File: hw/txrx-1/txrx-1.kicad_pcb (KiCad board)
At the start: 2 copper layers, 94 parts, among them J1 Conn_Coaxial, J2 Power, J4 Conn_01x07, U1 SN74CBT3253, U2 LM4562, U3 LM4562, U4 Si5351A-B-GT, U41 LM4562, U42 LM4562, U43 SN74CBT3253

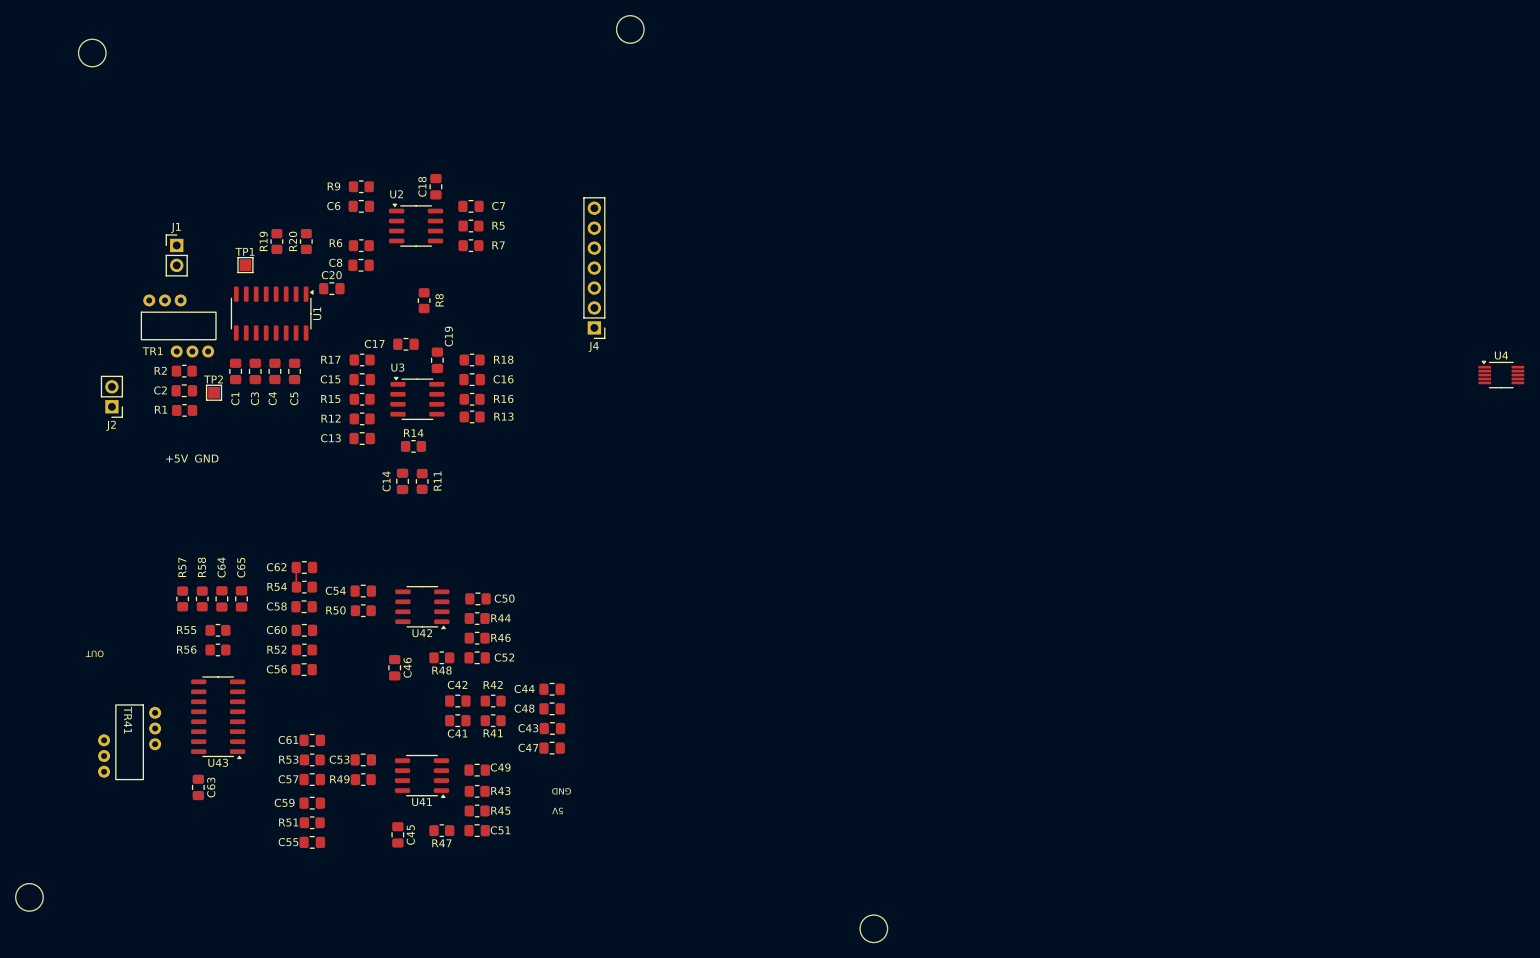
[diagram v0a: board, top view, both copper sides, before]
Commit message: Initial PCB layout for TXRX board
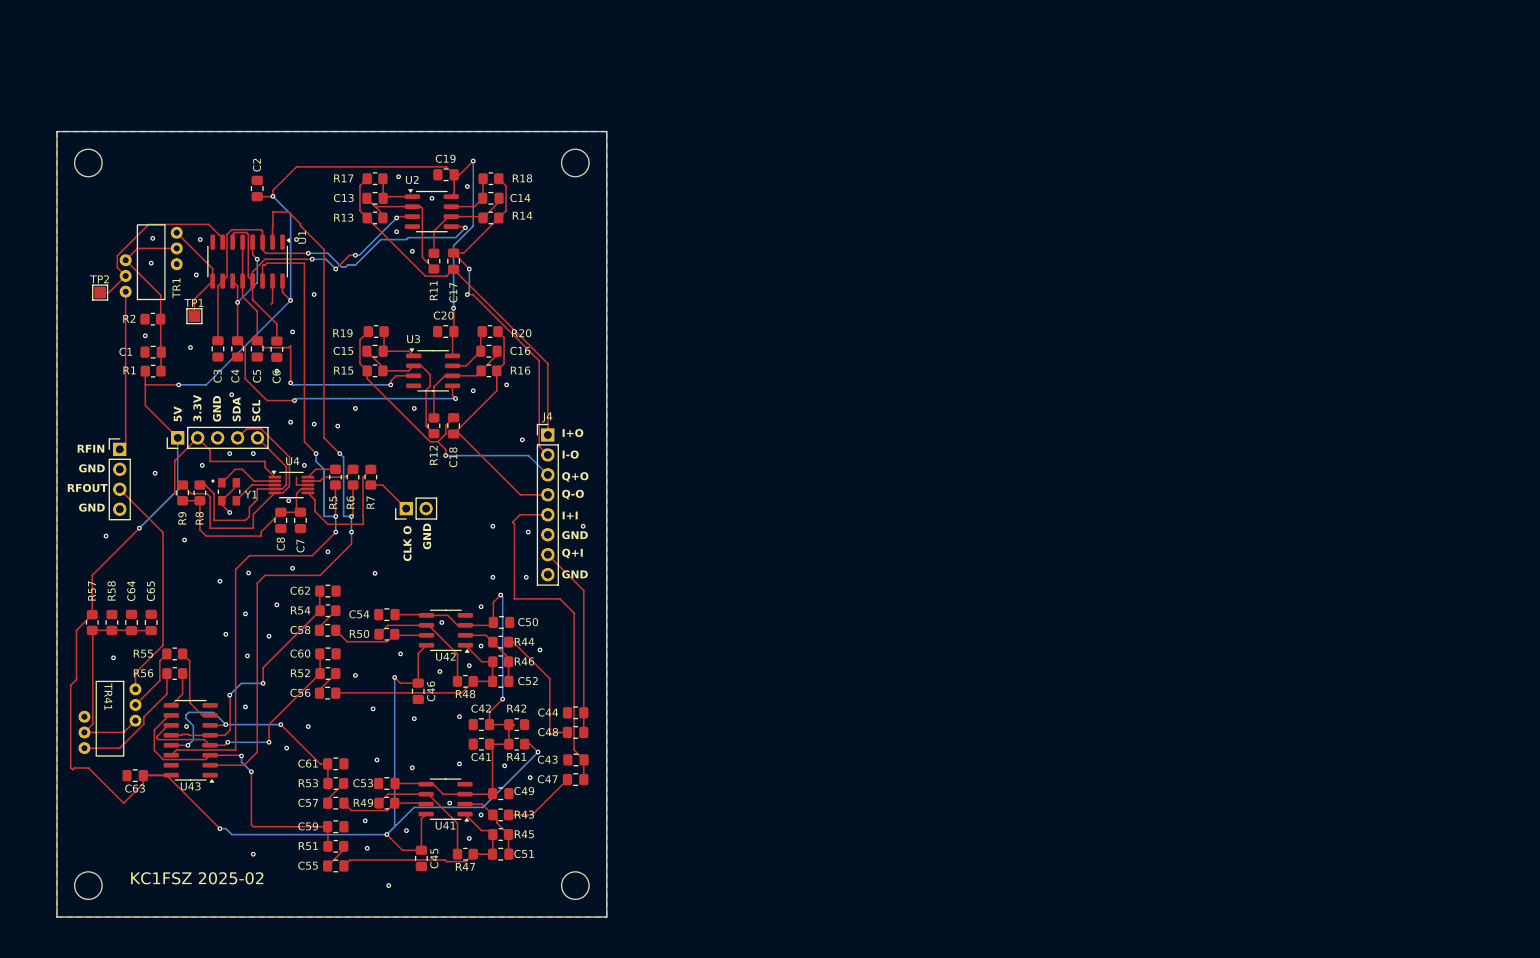
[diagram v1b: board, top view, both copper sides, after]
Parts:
- added J3: Conn_01x02, Connector_PinHeader_2.54mm:PinHeader_1x02_P2.54mm_Vertical, F.Cu at (74.5, 88.0)
- added Y1: CX3225SB25000D0FFFCC, bruce-footprints:OSCCC320X250X60N, F.Cu at (51.9, 85.9)
- J1: value Conn_Coaxial -> Conn_01x04; footprint Connector_PinHeader_2.54mm:PinHeader_1x02_P2.54mm_Vertical -> Connector_PinHeader_2.54mm:PinHeader_1x04_P2.54mm_Vertical
- J2: value Power -> Conn_01x05; footprint Connector_PinHeader_2.54mm:PinHeader_1x02_P2.54mm_Vertical -> Connector_PinHeader_2.54mm:PinHeader_1x05_P2.54mm_Vertical
- J4: value Conn_01x07 -> Conn_01x08; footprint Connector_PinHeader_2.54mm:PinHeader_1x07_P2.54mm_Vertical -> Connector_PinHeader_2.54mm:PinHeader_1x08_P2.54mm_Vertical
- moved U4 154.7 mm to (59.8, 85.0)
- moved C7 45.5 mm to (61.0, 89.5), turned to -90 degrees
- moved R9 45.1 mm to (46.0, 86.0), turned to 90 degrees
- moved H4 38.4 mm to (96.0, 136.0)
- moved C14 37.8 mm to (85.2, 48.5), turned to 180 degrees
- moved R8 37.6 mm to (48.2, 86.0)
- moved R5 36.3 mm to (65.5, 84.0), turned to -90 degrees
- moved C8 34.0 mm to (58.5, 89.5), turned to -90 degrees
- moved R7 32.1 mm to (70.0, 84.0), turned to -90 degrees
- moved R14 30.7 mm to (85.2, 51.0)
- moved C13 30.6 mm to (70.5, 48.5)
- moved C18 30.5 mm to (80.5, 77.5)
- moved R6 29.5 mm to (67.7, 84.0), turned to -90 degrees
- moved R13 28.2 mm to (70.5, 51.0)
- moved R11 28.1 mm to (78.0, 56.5)
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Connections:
- net I_MINUS renamed I_MINUS_OUT
- net I_PLUS renamed I_PLUS_OUT
- C18 pad 1: Q_MINUS -> Q_MINUS_OUT
- C18 pad 2: Q_PLUS -> Q_PLUS_OUT
- J1 pad 1: Net-(J1-In) -> RF_IN
- J2 pad 2: GND -> +3V3
- J4 pad 3: VCOML -> Q_PLUS_OUT
- J4 pad 4: Q_PLUS -> Q_MINUS_OUT
- J4 pad 5: Q_MINUS -> I_IN
- J4 pad 6: VCOMR -> GND
- J4 pad 7: GND -> Q_IN
- R15 pad 2: Q_PLUS -> Q_PLUS_OUT
- R16 pad 2: Q_MINUS -> Q_MINUS_OUT
- R19 pad 2: Q_PLUS -> Q_PLUS_OUT
- R20 pad 2: Q_MINUS -> Q_MINUS_OUT
- R9 pad 2: SCL -> SDA
- TR41 pad 1: TX_OUT -> RF_OUT
- U4 pad 5: SCL -> SDA
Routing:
- net +5V: track 0.00 -> 273.2 mm, vias 0 -> 10
- net CLK_Q: track 0.00 -> 98.7 mm, vias 0 -> 3
- net CLK_I: track 0.00 -> 94.4 mm, vias 0 -> 3
- net VBIAS: track 0.00 -> 62.3 mm, vias 0 -> 2
- net Net-(U1-1B4): track 0.00 -> 52.2 mm, vias 0 -> 2
- net Net-(U1-1B3): track 0.00 -> 51.9 mm, vias 0 -> 4
- net +3V3: track 0.00 -> 47.7 mm
- net I_PLUS_OUT: track 0.00 -> 46.2 mm
- net I_IN: track 0.00 -> 44.8 mm
- net I_MINUS_OUT: track 0.00 -> 44.7 mm, vias 0 -> 2
- net Net-(U1-1B1): track 0.00 -> 43.7 mm, vias 0 -> 4
- net Net-(U1-1B2): track 0.00 -> 39.4 mm, vias 0 -> 2
- net Q_PLUS_OUT: track 0.00 -> 39.2 mm, vias 0 -> 1
- net P0: track 0.00 -> 39.0 mm, vias 0 -> 2
- net SDA: track 0.00 -> 33.8 mm
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- added copper zone on B.Cu, net GND
- added copper zone on F.Cu, net GND
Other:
- board outline added: 70 x 100 mm
- board text added: "3.3V"
- board text added: "CLK O"
- board text added: "I+I"
- board text added: "I+O"
- board text added: "I-O"
- board text added: "KC1FSZ 2025-02"
- board text added: "Q+I"
- board text added: "Q+O"
- board text added: "Q-O"
- board text added: "RFIN"
- board text added: "RFOUT"
- board text added: "SCL"
- board text added: "SDA"
- board text removed: "+5V"
- board text removed: "OUT"

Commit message: Initial PCB layout for TXRX board
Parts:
- moved C2 17.9 mm to (60.2, 64.5), turned to -90 degrees
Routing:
- net +5V: track 273.2 -> 254.8 mm, vias 10 -> 9
- net P0: track 39.0 -> 38.5 mm, vias 2 -> 0
- net GND: vias 77 -> 90

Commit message: Final version being sent to fab
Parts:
- added R70: 0, Resistor_SMD:R_0805_2012Metric_Pad1.20x1.40mm_HandSolder, F.Cu at (66.5, 93.5)
- added R71: 0, Resistor_SMD:R_0805_2012Metric_Pad1.20x1.40mm_HandSolder, F.Cu at (69.5, 91.0)
- C64: value 4.7uF -> 10uF
- moved J3 37.2 mm to (38.0, 95.5), turned to 0 degrees
- moved C63 30.7 mm to (58.0, 97.2), turned to 90 degrees
- moved R7 29.5 mm to (43.0, 96.0), turned to 180 degrees
- moved R57 23.1 mm to (45.2, 123.0), turned to 90 degrees
- moved R58 21.3 mm to (42.8, 123.0), turned to -90 degrees
- moved C65 20.9 mm to (37.8, 123.0), turned to -90 degrees
- moved C64 20.5 mm to (40.2, 123.0), turned to -90 degrees
- moved C3 18.4 mm to (58.8, 51.2), turned to 90 degrees
- moved C6 16.7 mm to (61.0, 51.2), turned to 90 degrees
- moved R1 16.5 mm to (41.0, 54.0), turned to -90 degrees
- moved C4 16.5 mm to (54.2, 51.2), turned to 90 degrees
- moved C5 16.5 mm to (56.5, 51.2), turned to 90 degrees
- moved U43 14.7 mm to (53.0, 104.1), turned to 0 degrees
- moved C1 14.1 mm to (43.4, 54.0), turned to 90 degrees
- moved C2 12.1 mm to (49.0, 69.0), turned to 180 degrees
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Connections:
- U43 pad 14: CLK_I -> Net-(U43-S0)
- U43 pad 2: CLK_Q -> Net-(U43-S1)
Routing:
- net +5V: track 254.8 -> 33.5 mm, vias 9 -> 10
- net GND: track 10.5 -> 80.6 mm, vias 90 -> 95
- net CLK_Q: track 98.7 -> 34.8 mm, vias 3 -> 0
- net CLK_I: track 94.4 -> 36.8 mm, vias 3 -> 0
- net Net-(U43-S1): track 0.00 -> 26.0 mm
- net Net-(U43-S0): track 0.00 -> 21.0 mm
- net P270: track 32.0 -> 17.2 mm
- net +3V3: track 47.7 -> 35.5 mm
- net SDA: track 33.8 -> 22.8 mm
- net P90: track 32.3 -> 21.6 mm
- net Net-(U4-CLK2): track 17.0 -> 27.1 mm
- net Net-(U43-2A): track 4.66 -> 14.0 mm
- net SCL: track 25.7 -> 17.7 mm
- net Net-(R56-Pad2): track 16.5 -> 9.06 mm
- net I_IN: track 44.8 -> 38.0 mm
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- added copper zone on In2.Cu, net +5V
- added copper zone on In1.Cu, net GND
- removed copper zone on B.Cu, net GND
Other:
- copper layers 2 -> 4
- board text added: "CLK2"
- board text added: "bruce@mackinnon.com"
- board text removed: "CLK O"
